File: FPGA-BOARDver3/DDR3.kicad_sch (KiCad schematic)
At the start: 24 parts

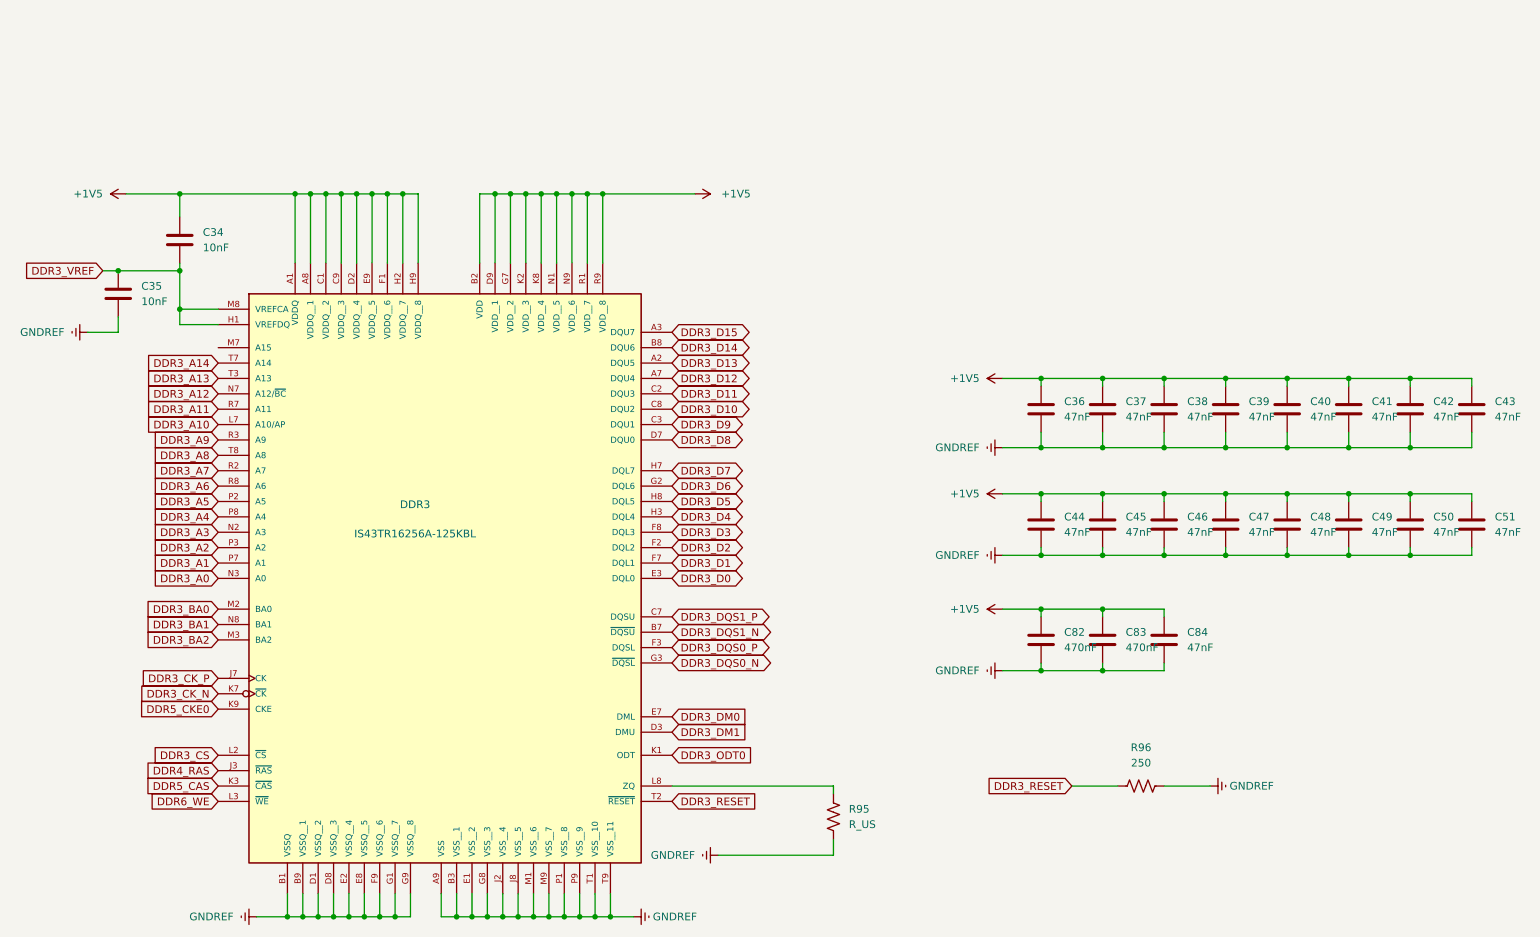
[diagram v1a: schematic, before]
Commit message: assigned footprints for power section and ddr3
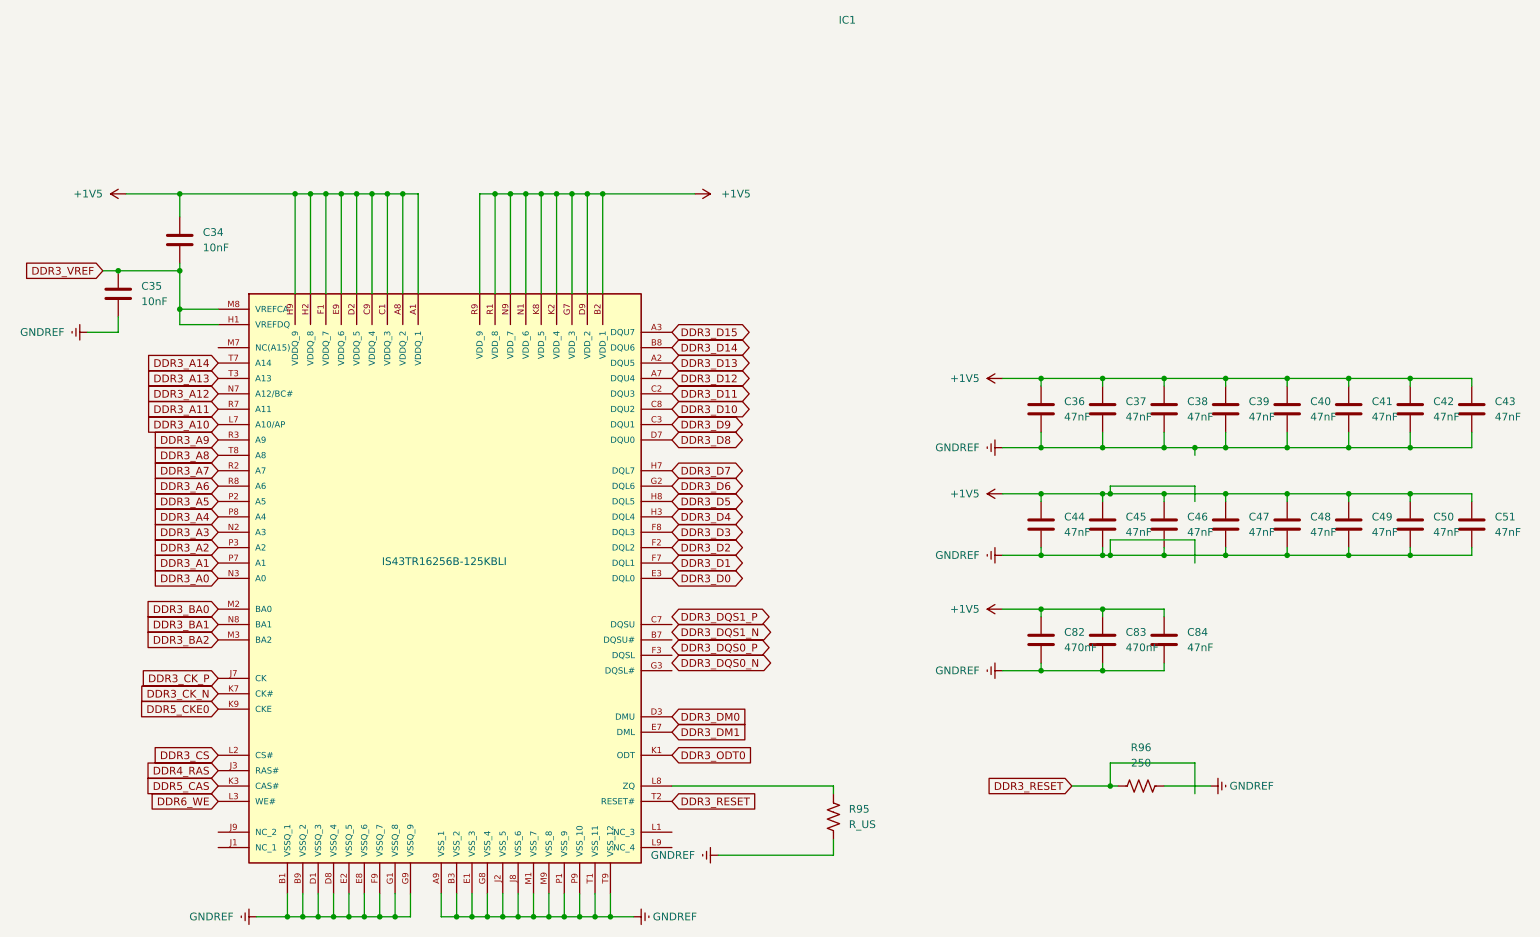
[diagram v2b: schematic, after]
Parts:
- removed DDR3: IS43TR16256A-125KBL, IS43TR16256A_125KBL:BGA96C80P9X16_900X1300X120, symbol IS43TR16256A-125KBL:IS43TR16256A-125KBL
- added IC1: IS43TR16256B-125KBLI, IS43TR16256B-125KBLI:BGA96C80P9X16_900X1300X120, symbol IS43TR16256B-125KBLI:IS43TR16256B-125KBLI
- C34, C35, C36, C37, C38, C39, C40, C41, C42, C43, C44, C45, C46, C47, C48, C49, C50, C51, C82, C83, C84: footprint (none) -> JLCPCB:C_0402
- R95, R96: footprint (none) -> JLCPCB:R_0402
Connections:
- net +1V5: now also IC1.A1 (VDDQ_1), IC1.A8 (VDDQ_2), IC1.B2 (VDD_1), IC1.C1 (VDDQ_3), IC1.C9 (VDDQ_4), IC1.D2 (VDDQ_5), IC1.D9 (VDD_2), IC1.E9 (VDDQ_6), IC1.F1 (VDDQ_7), IC1.G7 (VDD_3), IC1.H2 (VDDQ_8), IC1.H9 (VDDQ_9), IC1.K2 (VDD_4), IC1.K8 (VDD_5), IC1.N1 (VDD_6), IC1.N9 (VDD_7), IC1.R1 (VDD_8), IC1.R9 (VDD_9)
- net DDR3_A0: now also IC1.N3 (A0)
- net DDR3_A1: now also IC1.P7 (A1)
- net DDR3_A10: now also IC1.L7 (A10/AP)
- net DDR3_A11: now also IC1.R7 (A11)
- net DDR3_A12: now also IC1.N7 (A12/BC#)
- net DDR3_A13: now also IC1.T3 (A13)
- net DDR3_A14: now also IC1.T7 (A14)
- net DDR3_A2: now also IC1.P3 (A2)
- net DDR3_A3: now also IC1.N2 (A3)
- net DDR3_A4: now also IC1.P8 (A4)
- net DDR3_A5: now also IC1.P2 (A5)
- net DDR3_A6: now also IC1.R8 (A6)
- net DDR3_A7: now also IC1.R2 (A7)
- net DDR3_A8: now also IC1.T8 (A8)
- net DDR3_A9: now also IC1.R3 (A9)
- net DDR3_BA0: now also IC1.M2 (BA0)
- net DDR3_BA1: now also IC1.N8 (BA1)
- net DDR3_BA2: now also IC1.M3 (BA2)
- net DDR3_CK_N: now also IC1.K7 (CK#)
- net DDR3_CK_P: now also IC1.J7 (CK)
- net DDR3_CS: now also IC1.L2 (CS#)
- net DDR3_D0: now also IC1.E3 (DQL0)
- net DDR3_D1: now also IC1.F7 (DQL1)
- net DDR3_D10: now also IC1.C8 (DQU2)
- net DDR3_D11: now also IC1.C2 (DQU3)
- net DDR3_D12: now also IC1.A7 (DQU4)
- net DDR3_D13: now also IC1.A2 (DQU5)
- net DDR3_D14: now also IC1.B8 (DQU6)
- net DDR3_D15: now also IC1.A3 (DQU7)
- net DDR3_D2: now also IC1.F2 (DQL2)
- net DDR3_D3: now also IC1.F8 (DQL3)
- net DDR3_D4: now also IC1.H3 (DQL4)
- net DDR3_D5: now also IC1.H8 (DQL5)
- net DDR3_D6: now also IC1.G2 (DQL6)
- net DDR3_D7: now also IC1.H7 (DQL7)
- net DDR3_D8: now also IC1.D7 (DQU0)
- net DDR3_D9: now also IC1.C3 (DQU1)
- net DDR3_DM0: now also IC1.D3 (DMU)
- net DDR3_DM1: now also IC1.E7 (DML)
- net DDR3_ODT0: now also IC1.K1 (ODT)
- net DDR3_RESET: now also IC1.T2 (RESET#)
- net DDR3_VREF: now also IC1.H1 (VREFDQ), IC1.M8 (VREFCA)
- net DDR4_RAS: now also IC1.J3 (RAS#)
- net DDR5_CAS: now also IC1.K3 (CAS#)
- net DDR5_CKE0: now also IC1.K9 (CKE)
- net DDR6_WE: now also IC1.L3 (WE#)
- net GNDREF: now also IC1.A9 (VSS_1), IC1.B1 (VSSQ_1), IC1.B3 (VSS_2), IC1.B9 (VSSQ_2), IC1.D1 (VSSQ_3), IC1.D8 (VSSQ_4), IC1.E1 (VSS_3), IC1.E2 (VSSQ_5), IC1.E8 (VSSQ_6), IC1.F9 (VSSQ_7), IC1.G1 (VSSQ_8), IC1.G8 (VSS_4), IC1.G9 (VSSQ_9), IC1.J2 (VSS_5), IC1.J8 (VSS_6), IC1.M1 (VSS_7), IC1.M9 (VSS_8), IC1.P1 (VSS_9), IC1.P9 (VSS_10), IC1.T1 (VSS_11), IC1.T9 (VSS_12)
- net at R95.1: now also IC1.L8 (ZQ)

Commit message: footprints added to project specific library
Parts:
- C34, C35, C36, C37, C38, C39, C40, C41, C42, C43, C44, C45, C46, C47, C48, C49, C50, C51, C82, C83, C84: footprint JLCPCB:C_0402 -> footprints:C_0402
- IC1: footprint IS43TR16256B-125KBLI:BGA96C80P9X16_900X1300X120 -> footprints:BGA96C80P9X16_900X1300X120
- R95: footprint JLCPCB:R_0402 -> footprints:R_0402
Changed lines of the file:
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@@
 			)
 		)
-		(property "Footprint" "JLCPCB:C_0402"
+		(property "Footprint" "footprints:C_0402"
 			(at 204.1652 66.04 0)
 			(effects
@@
 			)
 		)
-		(property "Footprint" "JLCPCB:C_0402"
+		(property "Footprint" "footprints:C_0402"
 			(at 234.6452 85.09 0)
 			(effects
@@
 			)
 		)
-		(property "Footprint" "JLCPCB:C_0402"
+		(property "Footprint" "footprints:C_0402"
 			(at 41.6052 38.1 0)
 			(effects
@@
 			)
 		)
-		(property "Footprint" "JLCPCB:C_0402"
+		(property "Footprint" "footprints:C_0402"
 			(at 183.8452 66.04 0)
 			(effects
@@
 			)
 		)
-		(property "Footprint" "JLCPCB:C_0402"
+		(property "Footprint" "footprints:C_0402"
 			(at 244.8052 85.09 0)
 			(effects
@@
 			)
 		)
-		(property "Footprint" "JLCPCB:C_0402"
+		(property "Footprint" "footprints:C_0402"
 			(at 183.8452 104.14 0)
 			(effects
@@
 			)
 		)
-		(property "Footprint" "JLCPCB:C_0402"
+		(property "Footprint" "footprints:C_0402"
 			(at 254.9652 85.09 0)
 			(effects
@@
 			)
 		)
-		(property "Footprint" "JLCPCB:C_0402"
+		(property "Footprint" "footprints:C_0402"
 			(at 214.3252 85.09 0)
 			(effects
@@
 			)
 		)
-		(property "Footprint" "JLCPCB:C_0402"
+		(property "Footprint" "footprints:C_0402"
 			(at 214.3252 66.04 0)
 			(effects
@@
 			)
 		)
-		(property "Footprint" "JLCPCB:C_0402"
+		(property "Footprint" "footprints:C_0402"
 			(at 194.0052 66.04 0)
 			(effects
@@
 			)
 		)
-		(property "Footprint" "JLCPCB:C_0402"
+		(property "Footprint" "footprints:C_0402"
 			(at 183.8452 85.09 0)
 			(effects
@@
 			)
 		)
-		(property "Footprint" "JLCPCB:C_0402"
+		(property "Footprint" "footprints:C_0402"
 			(at 31.4452 46.99 0)
 			(effects
@@
 			)
 		)
-		(property "Footprint" "JLCPCB:R_0402"
+		(property "Footprint" "footprints:R_0402"
 			(at 149.606 129.794 90)
 			(effects
@@
 			)
 		)
-		(property "Footprint" "JLCPCB:C_0402"
+		(property "Footprint" "footprints:C_0402"
 			(at 224.4852 85.09 0)
 			(effects
@@
 			)
 		)
-		(property "Footprint" "JLCPCB:C_0402"
+		(property "Footprint" "footprints:C_0402"
 			(at 194.0052 85.09 0)
 			(effects
@@
 			)
 		)
-		(property "Footprint" "JLCPCB:C_0402"
+		(property "Footprint" "footprints:C_0402"
 			(at 254.9652 66.04 0)
 			(effects
@@
 			)
 		)
-		(property "Footprint" "IS43TR16256B-125KBLI:BGA96C80P9X16_900X1300X120"
+		(property "Footprint" "footprints:BGA96C80P9X16_900X1300X120"
 			(at 133.096 5.588 0)
 			(effects
@@
 			)
 		)
-		(property "Footprint" "JLCPCB:C_0402"
+		(property "Footprint" "footprints:C_0402"
 			(at 194.0052 104.14 0)
 			(effects
@@
 			)
 		)
-		(property "Footprint" "JLCPCB:C_0402"
+		(property "Footprint" "footprints:C_0402"
 			(at 224.4852 66.04 0)
 			(effects
@@
 			)
 		)
-		(property "Footprint" "JLCPCB:C_0402"
+		(property "Footprint" "footprints:C_0402"
 			(at 244.8052 66.04 0)
 			(effects
@@
 			)
 		)
-		(property "Footprint" "JLCPCB:C_0402"
+		(property "Footprint" "footprints:C_0402"
 			(at 234.6452 66.04 0)
 			(effects
@@
 			)
 		)
-		(property "Footprint" "JLCPCB:C_0402"
+		(property "Footprint" "footprints:C_0402"
 			(at 204.1652 104.14 0)
 			(effects
@@
 			)
 		)
-		(property "Footprint" "JLCPCB:C_0402"
+		(property "Footprint" "footprints:C_0402"
 			(at 204.1652 85.09 0)
 			(effects

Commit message: added symbol and footprint folders for common components in schematics
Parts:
- R96: footprint JLCPCB:R_0402 -> footprints:R_0402
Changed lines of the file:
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@@
 			)
 		)
-		(property "Footprint" "JLCPCB:R_0402"
+		(property "Footprint" "footprints:R_0402"
 			(at 199.644 123.444 90)
 			(effects

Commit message: update
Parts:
- R95: value R_US -> 240 1%
- R96: value 250 -> 4.7K
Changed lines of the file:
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@@
 	)
 	(junction
-		(at 208.28 68.58)
-		(diameter 0)
-		(color 0 0 0 0)
-	)
-	(junction
 		(at 72.39 26.67)
 		(diameter 0)
@@
 	)
 	(junction
-		(at 194.31 76.2)
-		(diameter 0)
-		(color 0 0 0 0)
-	)
-	(junction
 		(at 243.84 76.2)
 		(diameter 0)
@@
 	)
 	(junction
-		(at 194.31 86.36)
-		(diameter 0)
-		(color 0 0 0 0)
-	)
-	(junction
 		(at 110.49 26.67)
 		(diameter 0)
@@
 	(wire
 		(pts
-			(xy 208.28 68.58) (xy 213.36 68.58)
+			(xy 203.2 68.58) (xy 213.36 68.58)
 		)
 		(stroke
@@
 	(wire
 		(pts
-			(xy 194.31 83.82) (xy 194.31 86.36)
-		)
-		(stroke
-			(width 0)
-			(type default)
-		)
-	)
-	(wire
-		(pts
 			(xy 176.53 76.2) (xy 182.88 76.2)
 		)
@@
 	(wire
 		(pts
-			(xy 194.31 86.36) (xy 203.2 86.36)
+			(xy 193.04 86.36) (xy 203.2 86.36)
 		)
 		(stroke
@@
 	(wire
 		(pts
-			(xy 194.31 74.93) (xy 194.31 76.2)
-		)
-		(stroke
-			(width 0)
-			(type default)
-		)
-	)
-	(wire
-		(pts
 			(xy 99.06 146.05) (xy 101.6 146.05)
 		)
@@
 	(wire
 		(pts
-			(xy 208.28 83.82) (xy 208.28 87.63)
-		)
-		(stroke
-			(width 0)
-			(type default)
-		)
-	)
-	(wire
-		(pts
 			(xy 254 76.2) (xy 243.84 76.2)
 		)
@@
 	(wire
 		(pts
-			(xy 193.04 76.2) (xy 194.31 76.2)
-		)
-		(stroke
-			(width 0)
-			(type default)
-		)
-	)
-	(wire
-		(pts
 			(xy 74.93 26.67) (xy 72.39 26.67)
 		)
@@
 	(wire
 		(pts
-			(xy 208.28 74.93) (xy 194.31 74.93)
-		)
-		(stroke
-			(width 0)
-			(type default)
-		)
-	)
-	(wire
-		(pts
 			(xy 71.12 146.05) (xy 73.66 146.05)
 		)
@@
 	(wire
 		(pts
-			(xy 203.2 68.58) (xy 208.28 68.58)
-		)
-		(stroke
-			(width 0)
-			(type default)
-		)
-	)
-	(wire
-		(pts
 			(xy 203.2 104.14) (xy 203.2 105.41)
 		)
@@
 	(wire
 		(pts
-			(xy 208.28 69.85) (xy 208.28 68.58)
-		)
-		(stroke
-			(width 0)
-			(type default)
-		)
-	)
-	(wire
-		(pts
-			(xy 208.28 83.82) (xy 194.31 83.82)
-		)
-		(stroke
-			(width 0)
-			(type default)
-		)
-	)
-	(wire
-		(pts
 			(xy 105.41 26.67) (xy 105.41 43.18)
 		)
@@
 	(wire
 		(pts
-			(xy 208.28 77.47) (xy 208.28 74.93)
-		)
-		(stroke
-			(width 0)
-			(type default)
-		)
-	)
-	(wire
-		(pts
 			(xy 97.79 26.67) (xy 97.79 43.18)
 		)
@@
 	(wire
 		(pts
-			(xy 193.04 86.36) (xy 194.31 86.36)
-		)
-		(stroke
-			(width 0)
-			(type default)
-		)
-	)
-	(wire
-		(pts
 			(xy 203.2 66.04) (xy 203.2 68.58)
 		)
@@
 	(wire
 		(pts
-			(xy 194.31 76.2) (xy 203.2 76.2)
+			(xy 193.04 76.2) (xy 203.2 76.2)
 		)
 		(stroke
@@
 			)
 		)
-		(property "Value" "R_US"
+		(property "Value" "240 1%"
 			(at 151.13 130.8099 0)
 			(effects
@@
 			)
 		)
-		(property "Value" "250"
+		(property "Value" "4.7K"
 			(at 199.39 120.65 90)
 			(effects

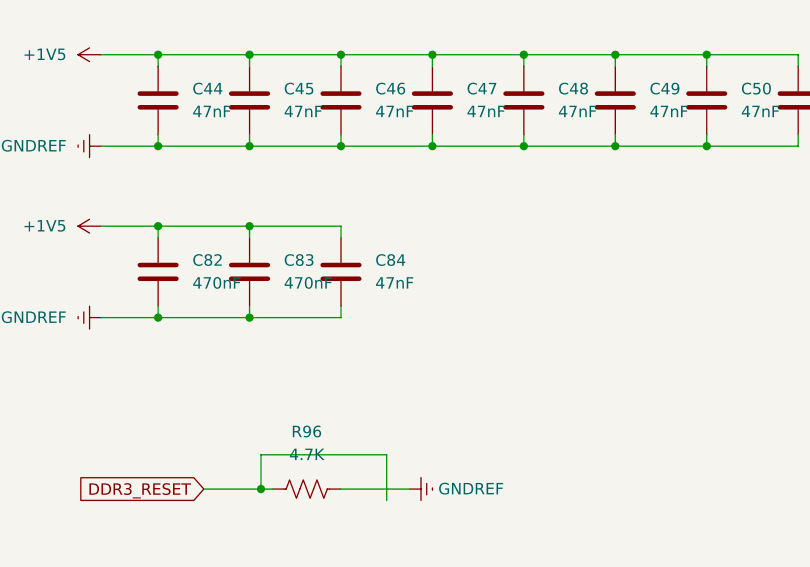
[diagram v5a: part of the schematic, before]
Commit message: added audio out and usb
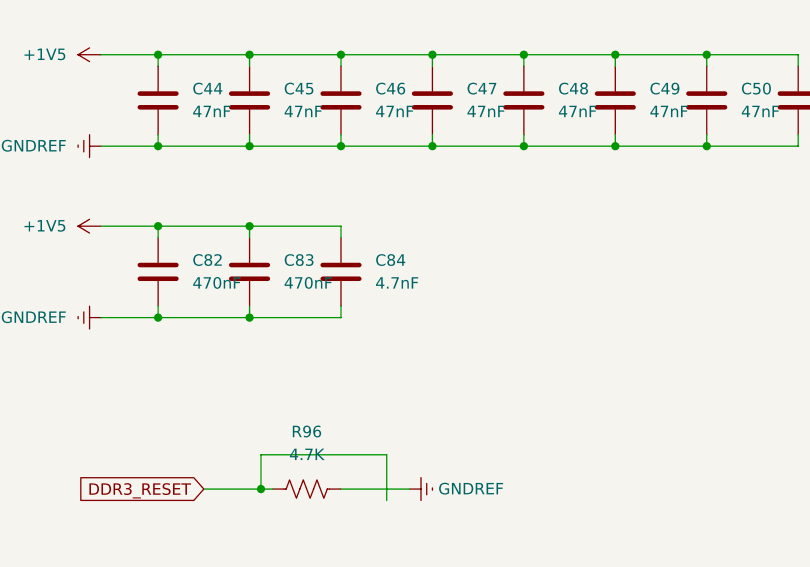
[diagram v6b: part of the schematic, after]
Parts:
- C84: value 47nF -> 4.7nF
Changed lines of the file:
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@@
 			)
 		)
+		(property "lcsc#" ""
+			(at 203.2 62.23 0)
+			(effects
+				(font
+					(size 1.27 1.27)
+				)
+				(hide yes)
+			)
+		)
 		(pin "2"
 		)
@@
 			)
 		)
+		(property "lcsc#" ""
+			(at 233.68 81.28 0)
+			(effects
+				(font
+					(size 1.27 1.27)
+				)
+				(hide yes)
+			)
+		)
 		(pin "2"
 		)
@@
 			)
 		)
+		(property "lcsc#" ""
+			(at 40.64 34.29 0)
+			(effects
+				(font
+					(size 1.27 1.27)
+				)
+				(hide yes)
+			)
+		)
 		(pin "1"
 		)
@@
 			)
 		)
+		(property "lcsc#" ""
+			(at 182.88 62.23 0)
+			(effects
+				(font
+					(size 1.27 1.27)
+				)
+				(hide yes)
+			)
+		)
 		(pin "2"
 		)
@@
 			)
 		)
+		(property "lcsc#" ""
+			(at 243.84 81.28 0)
+			(effects
+				(font
+					(size 1.27 1.27)
+				)
+				(hide yes)
+			)
+		)
 		(pin "2"
 		)
@@
 			)
 		)
+		(property "lcsc#" ""
+			(at 182.88 100.33 0)
+			(effects
+				(font
+					(size 1.27 1.27)
+				)
+				(hide yes)
+			)
+		)
 		(pin "2"
 		)
@@
 			)
 		)
+		(property "lcsc#" ""
+			(at 254 81.28 0)
+			(effects
+				(font
+					(size 1.27 1.27)
+				)
+				(hide yes)
+			)
+		)
 		(pin "2"
 		)
@@
 			)
 		)
+		(property "lcsc#" ""
+			(at 213.36 81.28 0)
+			(effects
+				(font
+					(size 1.27 1.27)
+				)
+				(hide yes)
+			)
+		)
 		(pin "2"
 		)
@@
 			)
 		)
+		(property "lcsc#" ""
+			(at 213.36 62.23 0)
+			(effects
+				(font
+					(size 1.27 1.27)
+				)
+				(hide yes)
+			)
+		)
 		(pin "2"
 		)
@@
 			)
 		)
+		(property "lcsc#" ""
+			(at 193.04 62.23 0)
+			(effects
+				(font
+					(size 1.27 1.27)
+				)
+				(hide yes)
+			)
+		)
 		(pin "2"
 		)
@@
 			)
 		)
+		(property "lcsc#" ""
+			(at 182.88 81.28 0)
+			(effects
+				(font
+					(size 1.27 1.27)
+				)
+				(hide yes)
+			)
+		)
 		(pin "2"
 		)
@@
 			)
 		)
+		(property "lcsc#" ""
+			(at 30.48 43.18 0)
+			(effects
+				(font
+					(size 1.27 1.27)
+				)
+				(hide yes)
+			)
+		)
 		(pin "1"
 		)
@@
 			)
 		)
+		(property "lcsc#" ""
+			(at 148.59 129.54 0)
+			(effects
+				(font
+					(size 1.27 1.27)
+				)
+				(hide yes)
+			)
+		)
 		(pin "2"
 		)
@@
 			)
 		)
+		(property "lcsc#" ""
+			(at 223.52 81.28 0)
+			(effects
+				(font
+					(size 1.27 1.27)
+				)
+				(hide yes)
+			)
+		)
 		(pin "2"
 		)
@@
 			)
 		)
+		(property "lcsc#" ""
+			(at 193.04 81.28 0)
+			(effects
+				(font
+					(size 1.27 1.27)
+				)
+				(hide yes)
+			)
+		)
 		(pin "2"
 		)
@@
 			)
 		)
+		(property "lcsc#" ""
+			(at 254 62.23 0)
+			(effects
+				(font
+					(size 1.27 1.27)
+				)
+				(hide yes)
+			)
+		)
 		(pin "2"
 		)
@@
 			)
 		)
+		(property "lcsc#" ""
+			(at 86.36 15.24 0)
+			(effects
+				(font
+					(size 1.27 1.27)
+				)
+				(hide yes)
+			)
+		)
 		(pin "E2"
 		)
@@
 			)
 		)
+		(property "lcsc#" ""
+			(at 199.39 124.46 0)
+			(effects
+				(font
+					(size 1.27 1.27)
+				)
+				(hide yes)
+			)
+		)
 		(pin "1"
 		)
@@
 			)
 		)
+		(property "lcsc#" ""
+			(at 193.04 100.33 0)
+			(effects
+				(font
+					(size 1.27 1.27)
+				)
+				(hide yes)
+			)
+		)
 		(pin "2"
 		)
@@
 			)
 		)
+		(property "lcsc#" ""
+			(at 223.52 62.23 0)
+			(effects
+				(font
+					(size 1.27 1.27)
+				)
+				(hide yes)
+			)
+		)
 		(pin "2"
 		)
@@
 			)
 		)
+		(property "lcsc#" ""
+			(at 243.84 62.23 0)
+			(effects
+				(font
+					(size 1.27 1.27)
+				)
+				(hide yes)
+			)
+		)
 		(pin "2"
 		)
@@
 			)
 		)
+		(property "lcsc#" ""
+			(at 233.68 62.23 0)
+			(effects
+				(font
+					(size 1.27 1.27)
+				)
+				(hide yes)
+			)
+		)
 		(pin "2"
 		)
@@
 			)
 		)
-		(property "Value" "47nF"
+		(property "Value" "4.7nF"
 			(at 207.01 101.5999 0)
 			(effects
@@
 			)
 		)
+		(property "lcsc#" ""
+			(at 203.2 100.33 0)
+			(effects
+				(font
+					(size 1.27 1.27)
+				)
+				(hide yes)
+			)
+		)
 		(pin "2"
 		)
@@
 			(at 203.2 81.28 0)
 			(effects
+				(font
+					(size 1.27 1.27)
+				)
+				(hide yes)
+			)
+		)
+		(property "lcsc#" ""
+			(at 203.2 81.28 0)
+			(effects
